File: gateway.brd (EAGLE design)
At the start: 100 x 146 mm, 72 parts, among them J1 RASPBERRYPI-40-PIN-GPIO_PTH_N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, Q1 BSS123

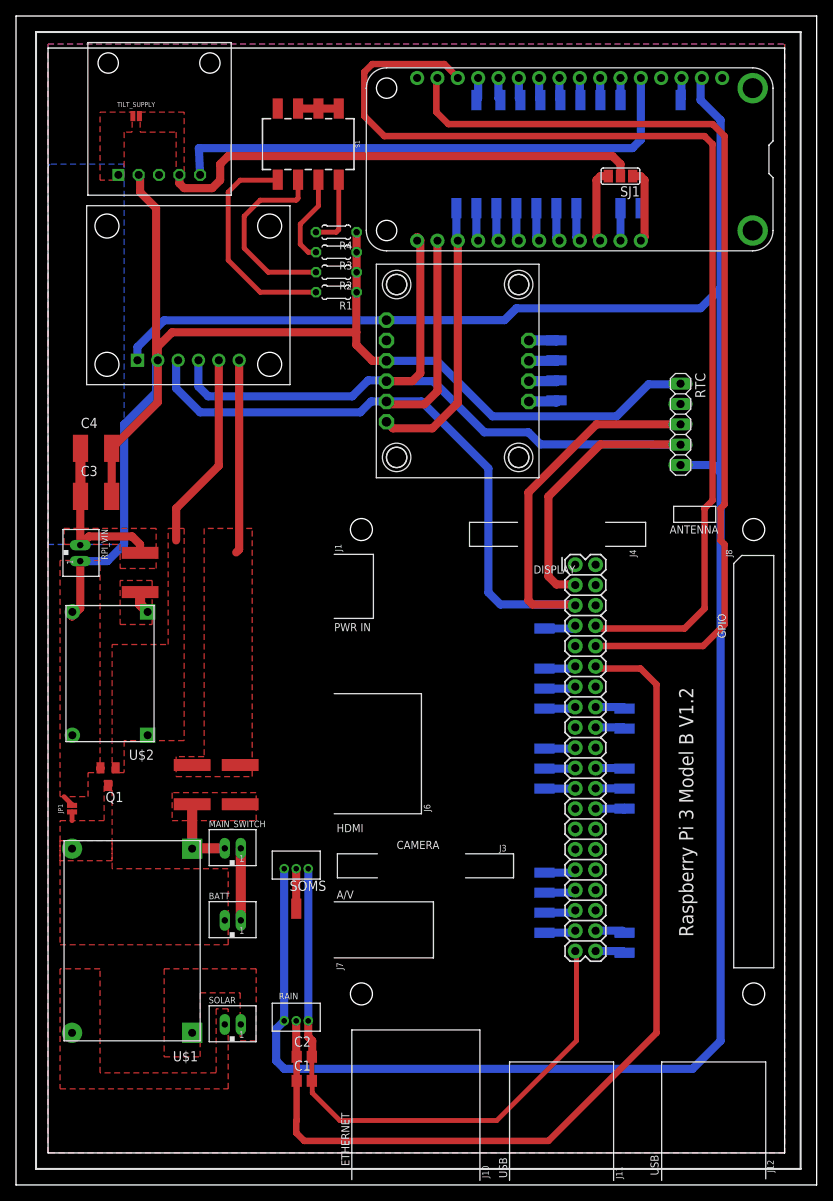
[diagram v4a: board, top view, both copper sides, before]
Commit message: edc modules - larger pad size for dcdc gateway - right package for capacitor and fuse tilt board - no more timer module, embedded design, right packages for caps and fuse
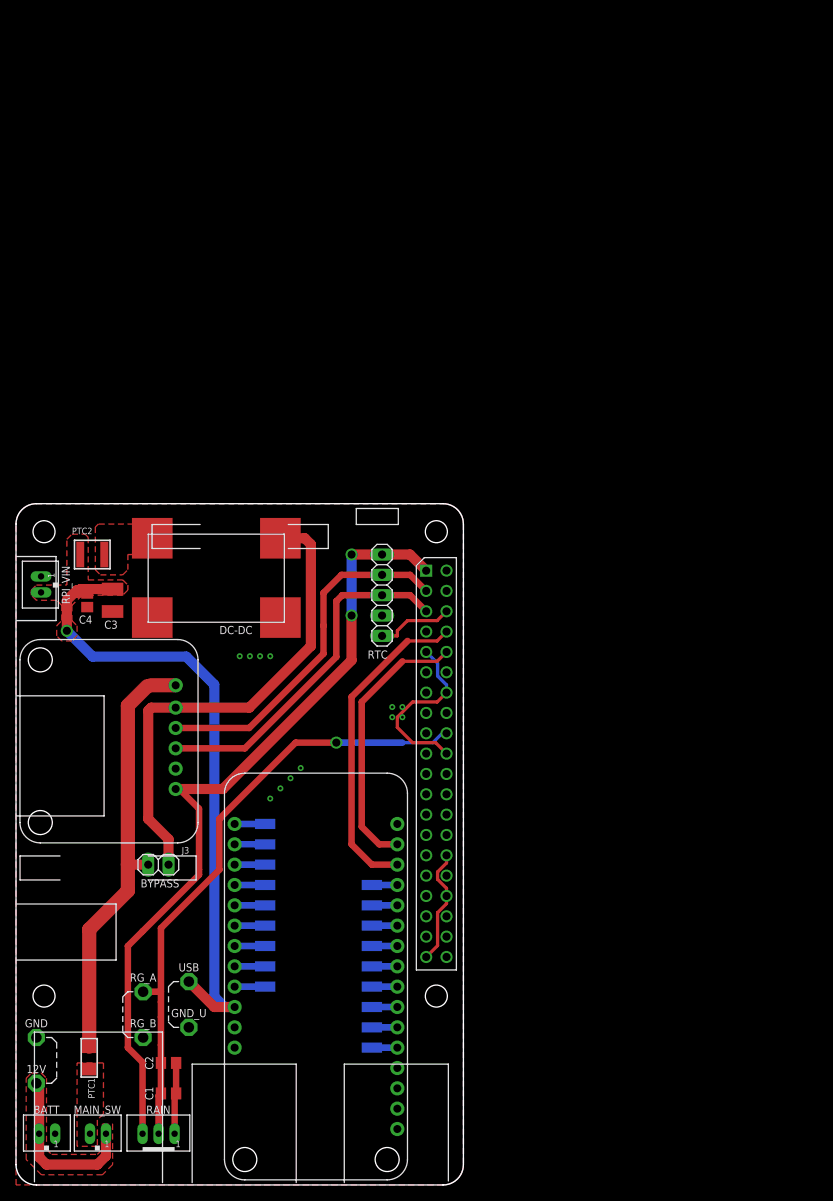
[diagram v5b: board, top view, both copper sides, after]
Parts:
- removed FUSE, FUSE1, FUSE2: MF-SMDF200, fuse:MF-SMDF050
- removed J1: RASPBERRYPI-40-PIN-GPIO_PTH_NO_SHROUD, SparkFun-Connectors:2X20
- removed JP1: JUMPER-SMT_2_NO_NO-SILK, SparkFun-Jumpers:SMT-JUMPER_2_NO_NO-SILK
- removed MAIN_SWITCH, SOLAR: JST-PH_2-PIN_HEADER, SRG:JST_B2B-PH_HEADER
- removed MS1: FEATHERWING_NODIM, adafruit:FEATHERWING_DIM
- removed PAD1, PAD10, PAD11, PAD12, PAD13, PAD14, PAD15, PAD16, PAD17, PAD18, PAD19, PAD2, PAD20, PAD21, PAD22, PAD23, PAD24, PAD25, PAD26, PAD27, PAD28, PAD29, PAD3, PAD30, PAD31, PAD32, PAD33, PAD34, PAD35, PAD36, PAD37, PAD38, PAD39, PAD4, PAD40, PAD41, PAD5, PAD6, PAD7, PAD8, PAD9: WIREPADSMD1,27-254, wirepad:SMD1,27-2,54
- removed Q1: BSS123, transistor-small-signal:SOT23
- removed R1, R2, R3, R4: (no value), rcl:0204/5
- removed S1: DIP-04SMD, SparkFun-Switches:DIPSWITCH-04-SMD
- removed SJ1: (no value), jumper:SJ_2
- removed SOMS: B3B-ZR, jst:B3B-ZR
- removed TILT_SUPPLY: (no value), SparkFun-Jumpers:SMT-JUMPER_2_NO_NO-SILK
- removed U$1: TP5100, edc_modules:TP5100
- removed U$2: MINI_360_BUCK, edc_modules:MINI_360_BUCK
- removed U$3: TPL5110_BREAKOUT, edc_modules:TPL5110_BREAKOUT
- removed U$4: BNO05_BREAKOUT, edc_modules:BNO05_BREAKOUT
- added 12V, GND, GND_U, RG_A, RG_B, USB: PTR1PAD1-13, testpad:P1-13
- added BYPASS: (no value), pinhead:1X02
- added DC-DC: MINI_360_BUCKMINI_360_BUCK_SMD, edc_modules:MINI_360_BUCK_SMD
- added IO10, IO11, IO12, IO13, IO5, IO6, IO9, IOA0, IOA1, IOA2, IOA3, IOA4, IOA5, MISO, MOSI, SCK, SCL, SDA: (no value), wirepad:SMD1,27-2,54
- added MAIN_SW: JST-PH_2-PIN_HEADER, SRG:JST_B2B-PH_HEADER
- added MS2: FEATHERWINGFEATHERWING_EDC, adafruit:FEATHERWING_NODIM_HOLES_2
- added PTC1: (no value), microbuilder:1206
- added PTC2: (no value), microbuilder:PTC1210
- C3: device rcl:C1812 -> rcl:C1210
- C4: device rcl:C1812 -> rcl:C2012
- INA219: value (none) -> INA219
- PCB2: value RPI3_NO_GPIO -> RPI3; device e14_Rpi3_RevA:RPI3_NO_GPIO -> e14_Rpi3_RevA:RPI3
- RAIN: value B3B-ZR -> JST-PH_3-PIN_HEADER; device jst:B3B-ZR -> SRG:JST_B3B-PH_HEADER
- moved INA219 57.2 mm to (22.7, 42.7), turned to 90 degrees
- moved RTC 43.0 mm to (45.7, 73.7), turned to 90 degrees
- moved PCB2 39.6 mm to (0.00, 85.1)
- moved BATT 35.3 mm to (3.81, 6.35)
- moved RAIN 22.3 mm to (17.8, 6.35), turned to 0 degrees
- moved C4 19.0 mm to (8.89, 73.0), turned to 270 degrees
- moved C1 17.0 mm to (19.1, 11.4)
- moved C2 17.0 mm to (19.1, 15.2)
- moved C3 13.1 mm to (12.1, 73.0), turned to 270 degrees
- moved RPI_VIN 6.29 mm to (3.17, 74.9), turned to 90 degrees
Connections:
- removed net 3.3V: J1.17
- removed net AREF: MS1.3, PAD13.1
- removed net BATT+: FUSE.1, FUSE1.1, MAIN_SWITCH.P2, U$1.VOUT+
- removed net BATT-: BATT.P2, JP1.1, Q1.3, U$1.VOUT-
- removed net CE0: J1.24, PAD4.1
- removed net CE1: J1.26, PAD5.1
- removed net DELAY: S1.5, S1.6, S1.7, S1.8, U$3.DELAY
- removed net DONE_PIN: MS1.5, U$3.DONE
- removed net EN: MS1.27, PAD29.1
- removed net FEATHER_3.3V: INA219.P$1, MS1.2, RAIN.3, RTC.5, SOMS.3, U$4.VIN
- removed net FEATHER_BAT: MS1.28, SJ1.1
- removed net FEATHER_SUPPLY: SJ1.2, TILT_SUPPLY.2, U$3.DRV
- removed net FEATHER_USB: MS1.26, SJ1.3
- removed net GP13: J1.33, PAD14.1
- removed net GP17: J1.11, PAD7.1
- removed net GP19: J1.35, PAD16.1
- removed net GP20: J1.38, PAD17.1
- removed net GP21: J1.40, PAD18.1
- removed net GP22: J1.15, PAD8.1
- removed net GP23: J1.16, PAD9.1
- removed net GP24: J1.18, PAD10.1
- removed net GP25: J1.22, PAD11.1
- removed net GP26: J1.37, PAD19.1
- removed net GP27: J1.13, PAD12.1
- removed net GP4: J1.7, PAD6.1
- removed net GP6: J1.31, PAD15.1
- removed net GPIO10: MS1.22, PAD33.1
- removed net GPIO11: MS1.23, PAD32.1
- removed net GPIO12: MS1.24, PAD31.1
- removed net GPIO13: MS1.25, PAD30.1
- removed net GPIO5: MS1.19, PAD36.1, U$4.RST
- removed net GPIO6: MS1.20, PAD35.1
- removed net GPIO9: MS1.21, PAD34.1
- removed net GPIOA1: MS1.6, PAD20.1
- removed net GPIOA2: MS1.7, PAD21.1
- removed net GPIOA3: MS1.8, PAD22.1
- removed net GPIOA4: MS1.9, PAD23.1
- removed net GPIOA5: MS1.10, PAD24.1
- removed net GPIOMISO: MS1.13, PAD26.1
- removed net GPIOMOSI: MS1.12, PAD27.1
- removed net GPIOSCK: MS1.11, PAD25.1
- removed net INA_VIN+: FUSE.2, FUSE1.2, INA219.P$6
- removed net INA_VIN-: INA219.P$5, Q1.1, U$2.IN+
- removed net MISO: J1.21, PAD2.1
- removed net MOSI: J1.19, PAD3.1
- removed net SCLK: J1.23, PAD1.1
- removed net SOLAR+: SOLAR.P1, U$1.VIN+
- removed net SOLAR-: SOLAR.P2, U$1.VIN-
- removed net VBAT: PAD28.1
- removed net VOLTAGE_SUPPLY: C3.1, C4.1, FUSE2.2, RPI_VIN.P2, TILT_SUPPLY.1, U$3.VDD
- new net +5V: C3.1, C4.1, MS2.26, PTC2.P$1, RPI_VIN.P2, USB.TP
- new net N$14: IO13.1, MS2.25
- new net N$16: MOSI.1, MS2.12
- new net N$17: MS2.11, SCK.1
- new net N$18: IOA5.1, MS2.10
- new net N$19: IOA4.1, MS2.9
- new net N$20: IOA3.1, MS2.8
- new net N$21: IOA2.1, MS2.7
- new net N$22: IOA1.1, MS2.6
- new net N$23: IOA0.1, MS2.5
- new net N$24: DC-DC.OUT+, PTC2.P$2
- net +3V3: now also INA219.1, PCB2.P$1, RAIN.P3, RTC.5; no longer J1.1
- net GND: now also BATT.P1, DC-DC.IN-, DC-DC.OUT-, GND.TP, GND_U.TP, INA219.2, MS2.4, PCB2.P$14, PCB2.P$20, PCB2.P$29, PCB2.P$30, PCB2.P$34, PCB2.P$39, PCB2.P$6, PCB2.P$9, RAIN.P1, RG_B.TP; no longer INA219.P$2, J1.14, J1.20, J1.25, J1.29, J1.30, J1.32, J1.34, J1.36, J1.39, J1.6, J1.9, JP1.2, MS1.4, Q1.2, R1.1, R2.1, R3.1, R4.1, RAIN.1, SOMS.1, U$2.IN-, U$2.OUT-, U$3.GND, U$4.GND
- net N$1: now also MS2.17, SDA.1; no longer PAD37.1, U$4.INT
- net N$10: now also IO9.1, MS2.21; no longer R2.2, S1.3
- net N$11: now also IO10.1, MS2.22; no longer R3.2, S1.2
- net N$12: now also IO11.1, MS2.23; no longer R4.2, S1.1
- net N$13: now also IO12.1, MS2.24; no longer BATT.P1, MAIN_SWITCH.P1
- net N$15: now also MISO.1, MS2.13; no longer PAD41.1, SOMS.2
- net N$2: now also 12V.TP, BATT.P2, MAIN_SW.P1; no longer J1.2
- net N$3: now also MAIN_SW.P2, PTC1.2; no longer J1.4
- net N$5: now also BYPASS.1, DC-DC.IN+, INA219.5; no longer PAD38.1, U$4.ADR
- net N$6: now also BYPASS.2, INA219.6, PTC1.1; no longer PAD39.1, U$4.PS0
- net N$7: now also MS2.18, SCL.1; no longer PAD40.1, U$4.PS1
- net N$8: now also IO5.1, MS2.19; no longer FUSE2.1, U$2.OUT+
- net N$9: now also IO6.1, MS2.20; no longer R1.2, S1.4
- net RPI_GPIO18: now also PCB2.P$18, RAIN.P2, RG_A.TP; no longer J1.12, RAIN.2
- net RPI_RX: now also MS2.15, PCB2.P$10; no longer J1.10, MS1.15
- net RPI_SCL: now also INA219.3, PCB2.P$5; no longer INA219.P$3, J1.5, MS1.18, U$4.SCL
- net RPI_SDA: now also INA219.4, PCB2.P$3; no longer INA219.P$4, J1.3, MS1.17, U$4.SDA
- net RPI_TX: now also MS2.14, PCB2.P$8; no longer J1.8, MS1.14
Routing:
- net FEATHER_3.3V: track 286.1 -> 0.00 mm
- net GND: track 250.9 -> 55.6 mm, vias 0 -> 12
- net +3V3: track 0.00 -> 101.0 mm, vias 0 -> 2
- net RPI_SCL: track 143.0 -> 44.1 mm
- net RPI_TX: track 136.5 -> 40.4 mm
- net RPI_RX: track 120.2 -> 34.1 mm
- net +5V: track 0.00 -> 82.1 mm, vias 0 -> 1
- net RPI_SDA: track 123.4 -> 44.5 mm
- net DONE_PIN: track 66.7 -> 0.00 mm
- net FEATHER_SUPPLY: track 61.1 -> 0.00 mm
- net N$5: track 3.59 -> 60.8 mm
- net N$6: track 3.48 -> 54.1 mm
- net RPI_GPIO18: track 120.1 -> 77.5 mm, vias 0 -> 1
- net GPIO5: track 35.0 -> 0.00 mm
- net INA_VIN-: track 24.7 -> 0.00 mm
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- added copper zone on layer 1, net +5V
- added copper zone on layer 1, net N$2
- added copper zone on layer 1, net N$24
- added copper zone on layer 1, net N$3
- removed copper zone on layer 1, net BATT+
- removed copper zone on layer 1, net BATT-
- removed copper zone on layer 1, net FEATHER_SUPPLY
- removed copper zone on layer 1, net INA_VIN+
- removed copper zone on layer 1, net INA_VIN-
- removed copper zone on layer 1, net N$8
- removed copper zone on layer 1, net SOLAR+
- removed copper zone on layer 1, net SOLAR-
- removed copper zone on layer 1, net VOLTAGE_SUPPLY
- removed copper zone on layer 16, net VOLTAGE_SUPPLY
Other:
- board size 100 x 146 mm -> 55.9 x 85.1 mm
- board text added: "IN"
- board text added: "OUT"
- board text added: "Slope Monitoring Gateway Board V2"

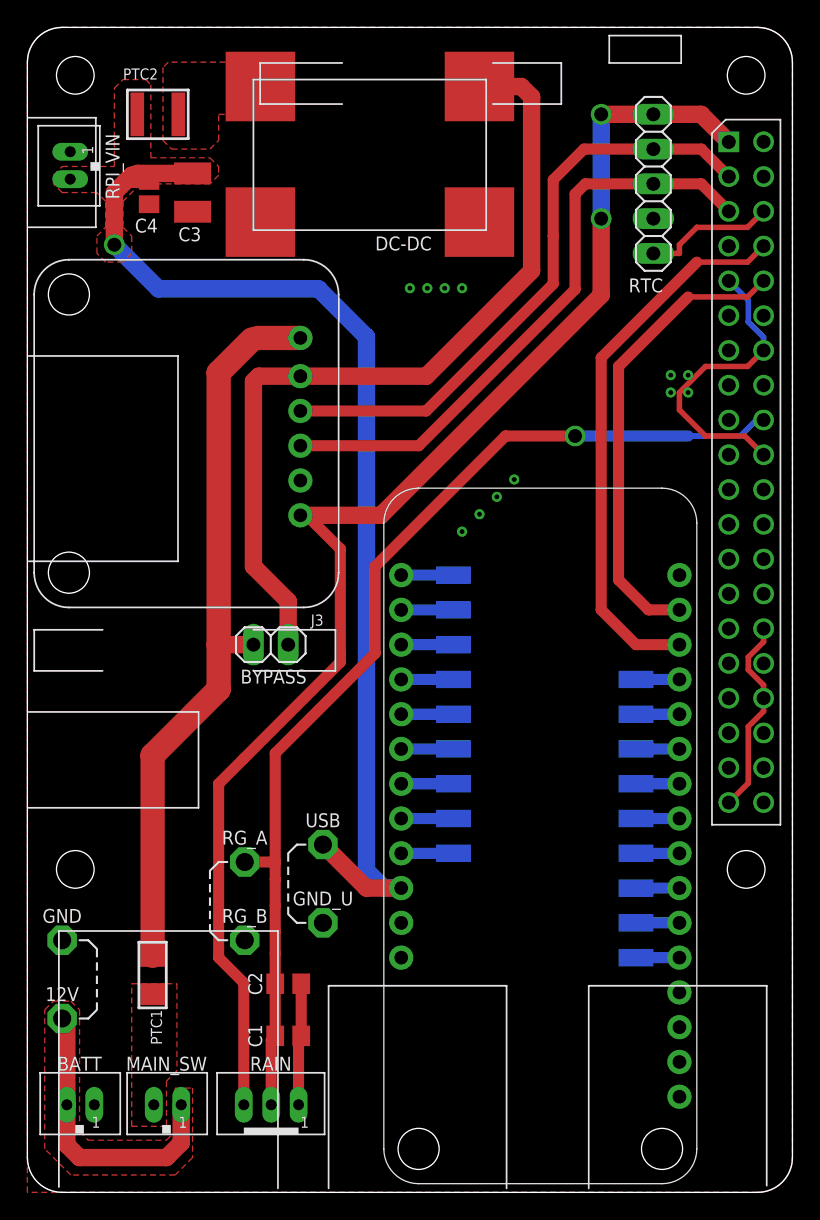
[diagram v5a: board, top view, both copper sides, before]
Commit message: new gateway versions
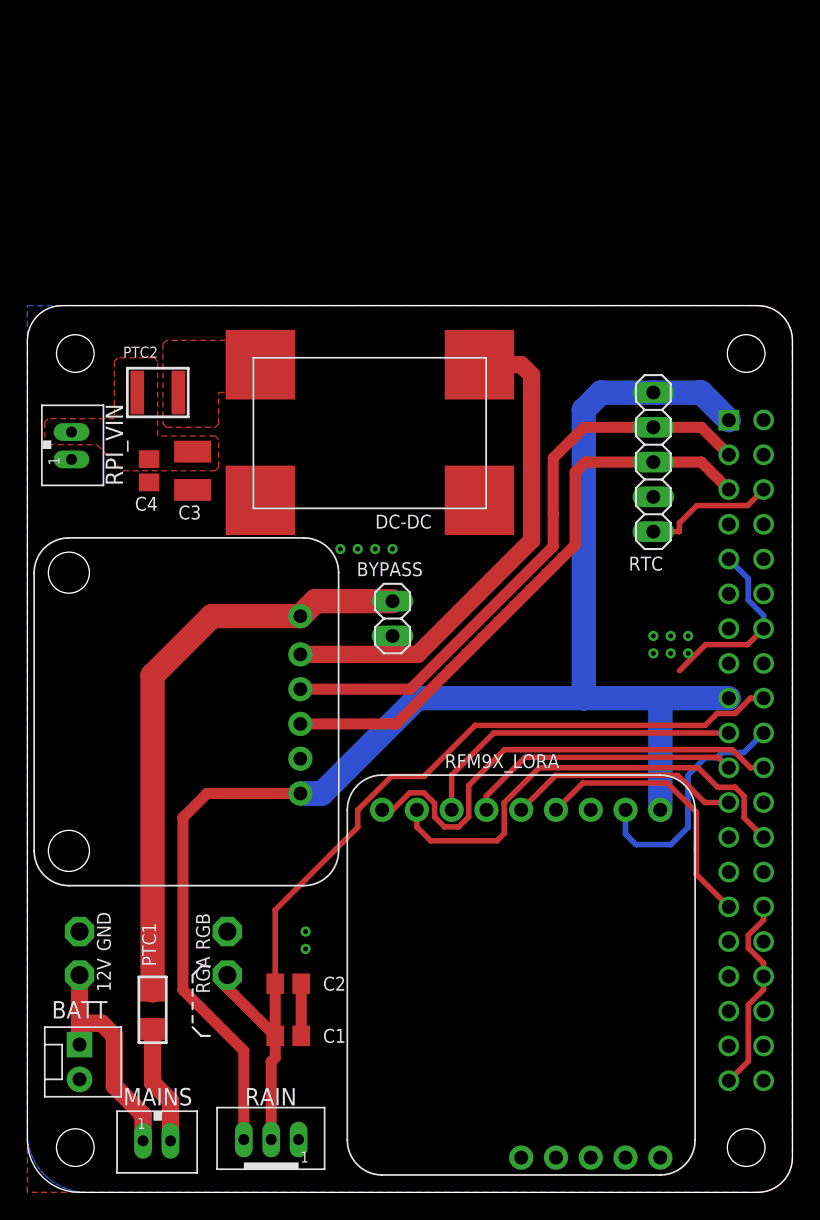
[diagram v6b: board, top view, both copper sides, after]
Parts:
- removed GND_U, RG_A, RG_B, USB: PTR1PAD1-13, testpad:P1-13
- removed IO10, IO11, IO12, IO13, IO5, IO6, IO9, IOA0, IOA1, IOA2, IOA3, IOA4, IOA5, MISO, MOSI, SCK, SCL, SDA: (no value), wirepad:SMD1,27-2,54
- removed MAIN_SW: JST-PH_2-PIN_HEADER, SRG:JST_B2B-PH_HEADER
- removed MS2: FEATHERWINGFEATHERWING_EDC, adafruit:FEATHERWING_NODIM_HOLES_2
- added MAINS: JST-PH_2-PIN_HEADER, SRG:JST_B2B-PH_HEADER
- added RFM9X_LORA: RFM9X_MODULE, edc_modules:RFM9X_MODULE
- added RGA, RGB: PTR1PAD1-13, testpad:P1-13
- BATT: value JST-PH_2-PIN_HEADER -> (none); device SRG:JST_B2B-PH_HEADER -> SparkFun-Connectors:MOLEX-1X2
- moved C3 20.3 mm to (12.1, 52.7)
- moved C4 20.3 mm to (8.89, 52.7)
- moved PCB2 20.3 mm to (0.00, 64.8)
- moved RPI_VIN 20.3 mm to (3.17, 54.6), turned to 270 degrees
- moved DC-DC 20.3 mm to (25.4, 55.9)
- moved INA219 20.3 mm to (22.7, 22.4)
- moved PTC2 20.3 mm to (9.53, 58.4)
- moved RTC 20.3 mm to (45.7, 53.3)
- moved BYPASS 9.09 mm to (26.7, 41.9), turned to 90 degrees
- moved BATT 4.45 mm to (3.81, 10.8), turned to 270 degrees
- moved 12V 3.42 mm to (3.81, 15.9)
- moved RAIN 2.54 mm to (17.8, 3.81)
- moved PTC1 2.54 mm to (9.14, 13.3)
- moved GND 1.42 mm to (3.81, 19.1)
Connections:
- removed net N$1: MS2.17, SDA.1
- removed net N$10: IO9.1, MS2.21
- removed net N$11: IO10.1, MS2.22
- removed net N$12: IO11.1, MS2.23
- removed net N$13: IO12.1, MS2.24
- removed net N$14: IO13.1, MS2.25
- removed net N$15: MISO.1, MS2.13
- removed net N$16: MOSI.1, MS2.12
- removed net N$17: MS2.11, SCK.1
- removed net N$18: IOA5.1, MS2.10
- removed net N$19: IOA4.1, MS2.9
- removed net N$20: IOA3.1, MS2.8
- removed net N$21: IOA2.1, MS2.7
- removed net N$22: IOA1.1, MS2.6
- removed net N$23: IOA0.1, MS2.5
- removed net N$7: MS2.18, SCL.1
- removed net N$8: IO5.1, MS2.19
- removed net N$9: IO6.1, MS2.20
- new net CE1: PCB2.P$26, RFM9X_LORA.8
- new net GPIO25: PCB2.P$22, RFM9X_LORA.9
- new net GPIO5: PCB2.P$29, RFM9X_LORA.4
- new net MISO: PCB2.P$21, RFM9X_LORA.6
- new net MOSI: PCB2.P$19, RFM9X_LORA.7
- new net SCK: PCB2.P$23, RFM9X_LORA.5
- net +3V3: now also PCB2.P$17, RFM9X_LORA.1
- net +5V: no longer MS2.26, USB.TP
- net GND: now also BATT.2, RFM9X_LORA.2, RGB.TP; no longer BATT.P1, GND_U.TP, MS2.4, PCB2.P$29, RG_B.TP
- net N$2: now also BATT.1, MAINS.P1; no longer BATT.P2, MAIN_SW.P1
- net N$3: now also MAINS.P2; no longer MAIN_SW.P2
- net RPI_GPIO18: now also RGA.TP; no longer RG_A.TP
- net RPI_RX: no longer MS2.15
- net RPI_TX: no longer MS2.14
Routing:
- net +5V: track 82.1 -> 0.00 mm, vias 1 -> 0
- net RPI_TX: track 40.4 -> 0.00 mm
- net GPIO25: track 0.00 -> 34.2 mm
- net RPI_RX: track 34.1 -> 0.00 mm
- net CE1: track 0.00 -> 33.6 mm
- net MOSI: track 0.00 -> 24.1 mm
- net N$5: track 60.8 -> 37.9 mm
- net MISO: track 0.00 -> 20.2 mm
- net GPIO5: track 0.00 -> 19.8 mm
- net SCK: track 0.00 -> 17.0 mm
- net RPI_GPIO18: track 77.5 -> 65.6 mm, vias 1 -> 0
- net N$6: track 54.1 -> 42.8 mm
- net +3V3: track 101.0 -> 110.3 mm, vias 2 -> 0
- net N$3: track 0.00 -> 8.71 mm
- net N$2: track 21.3 -> 16.5 mm
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- removed copper zone on layer 1, net N$2
- removed copper zone on layer 1, net N$3
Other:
- board size 55.9 x 85.1 mm -> 55.9 x 64.8 mm
- board text added: "Slope Monitoring Gateway Board V3"
- board text removed: "Slope Monitoring Gateway Board V2"
